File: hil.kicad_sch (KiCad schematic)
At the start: 29 parts, among them J1 5V In, J10 +3V3, J11 GND, J2 USB_B, J3 IO A, J4 IO B, J7 CAN, J8 I2C, J9 +5V, U1 MCP2515, U2 AZ1117-3.3, U3 MCP2562, Y1 16 MHz

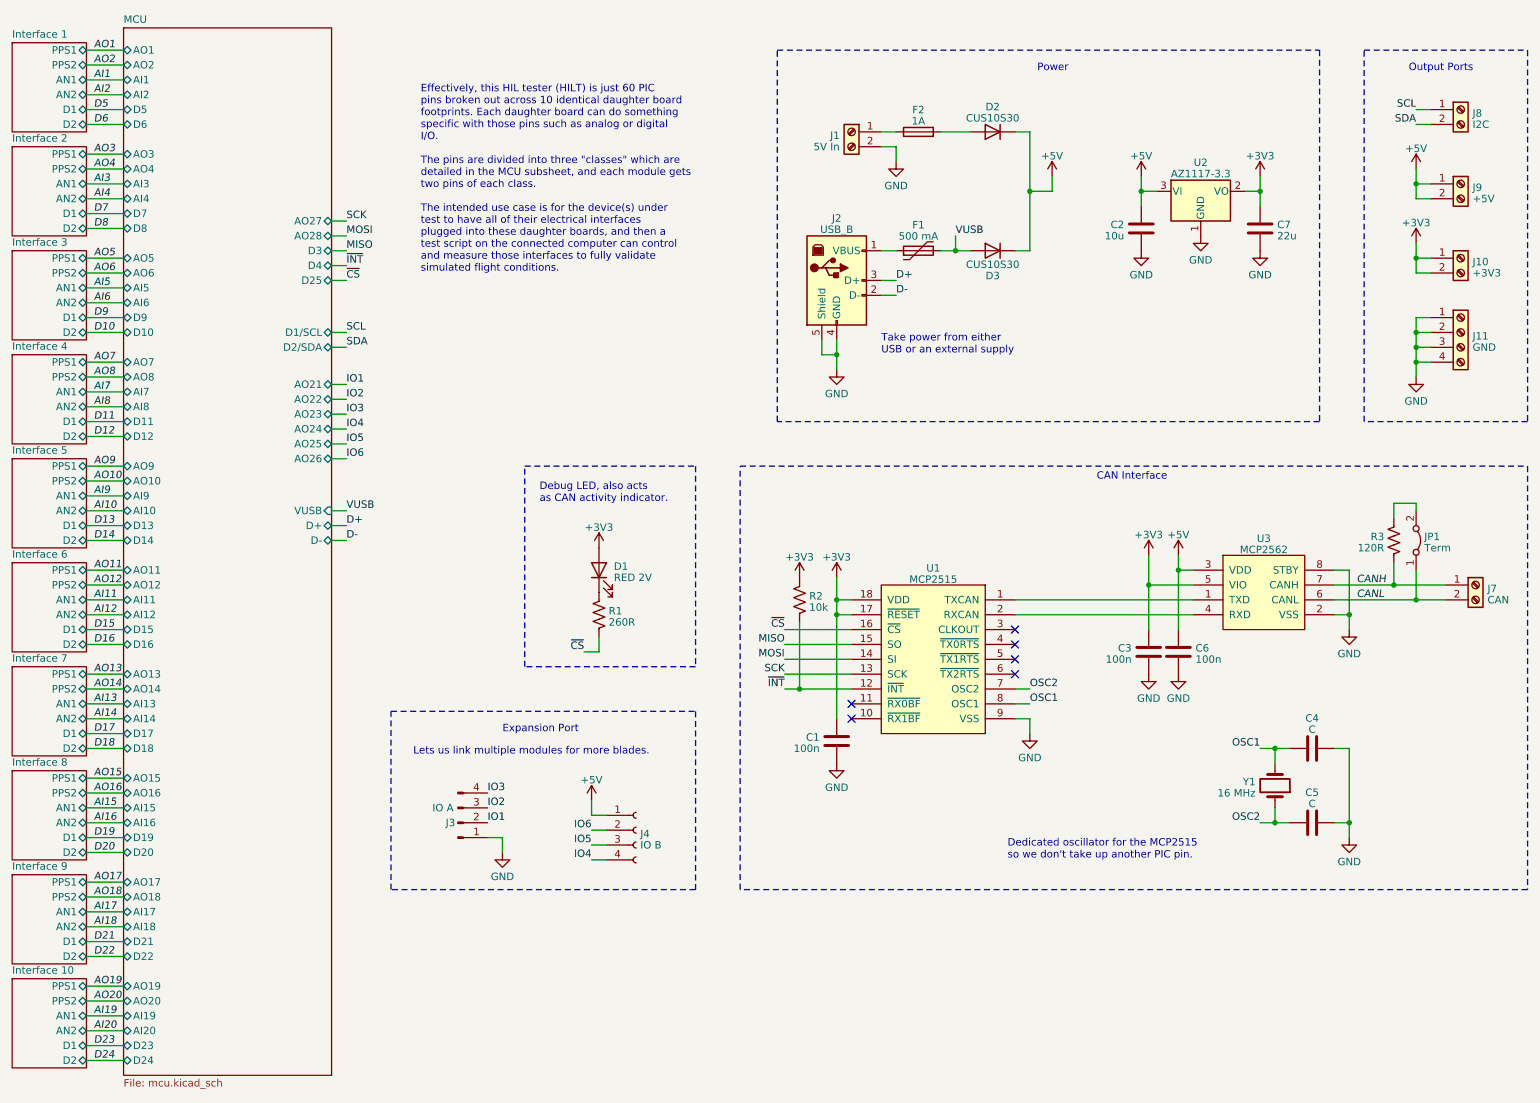
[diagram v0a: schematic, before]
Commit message: Address review comments, finish routing HILT main board
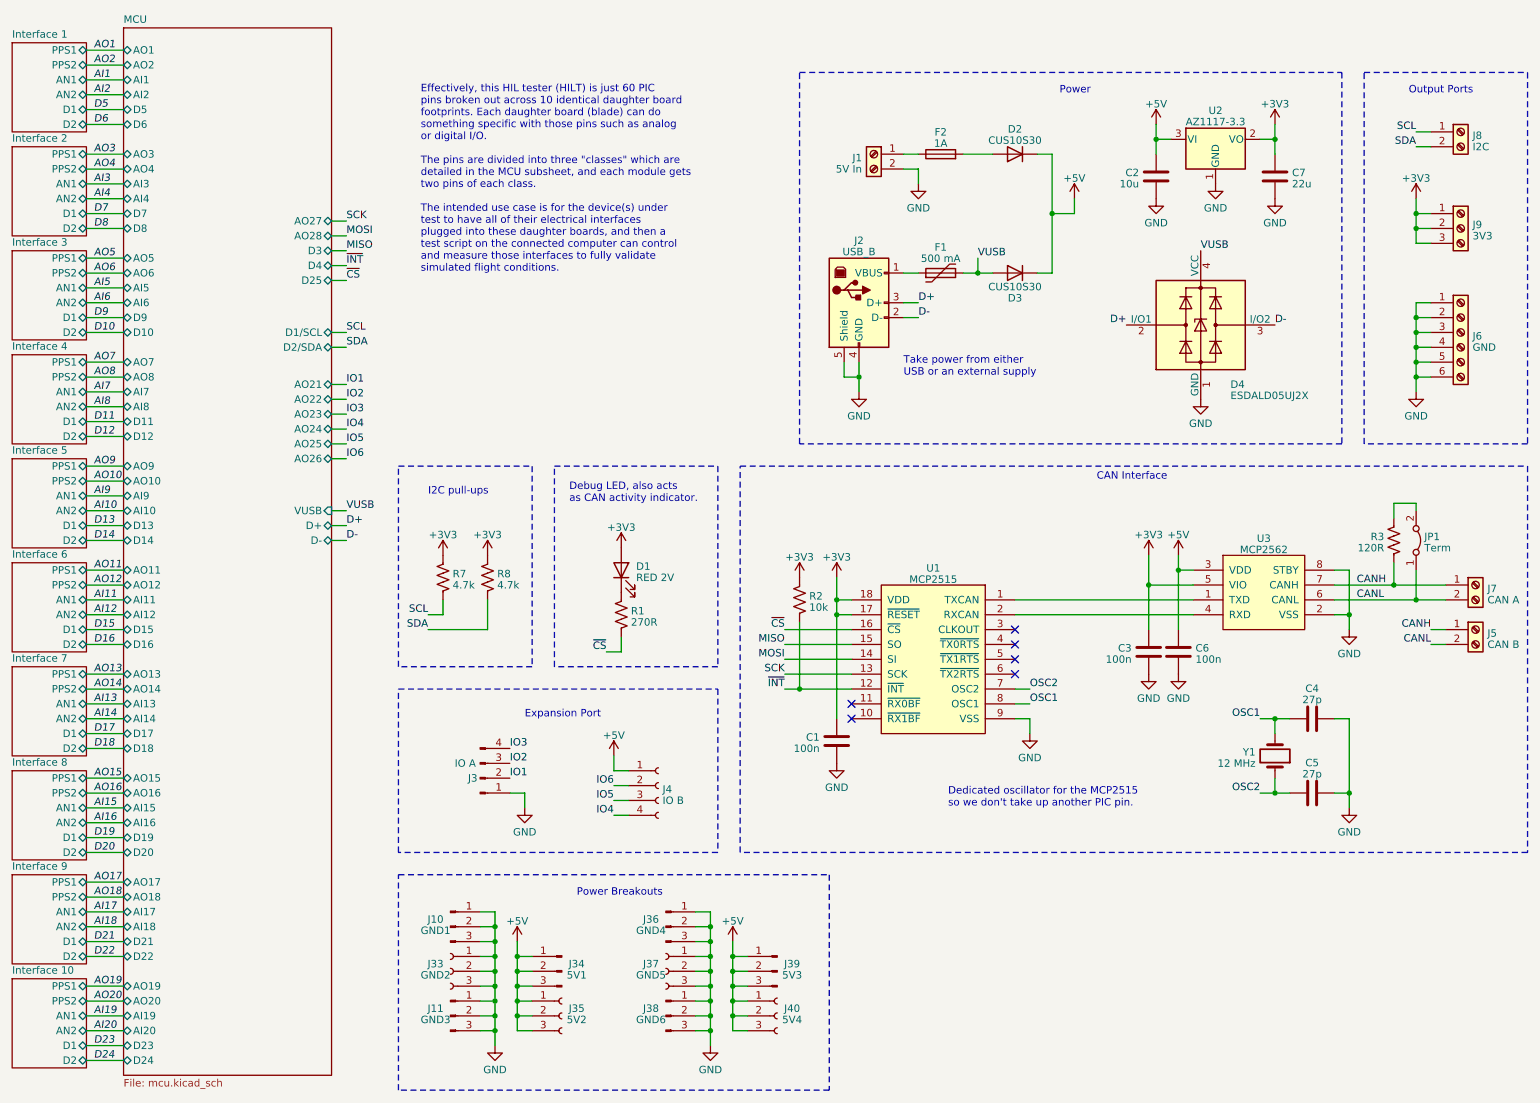
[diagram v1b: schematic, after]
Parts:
- removed J10: +3V3, TerminalBlock_Phoenix:TerminalBlock_Phoenix_PT-1,5-2-5.0-H_1x02_P5.00mm_Horizontal, symbol Connector:Screw_Terminal_01x02
- removed J11: GND, TerminalBlock_Phoenix:TerminalBlock_Phoenix_PT-1,5-4-5.0-H_1x04_P5.00mm_Horizontal, symbol Connector:Screw_Terminal_01x04
- removed J9: +5V, TerminalBlock_Phoenix:TerminalBlock_Phoenix_PT-1,5-2-5.0-H_1x02_P5.00mm_Horizontal, symbol Connector:Screw_Terminal_01x02
- added D4: ESDALD05UJ2X, Package_TO_SOT_SMD:SOT-143_Handsoldering, symbol Power_Protection:PRTR5V0U2X
- added J10: GND1, Connector_PinHeader_2.54mm:PinHeader_1x03_P2.54mm_Horizontal, symbol Connector:Conn_01x03_Pin
- added J11: GND3, Connector_PinHeader_2.54mm:PinHeader_1x03_P2.54mm_Horizontal, symbol Connector:Conn_01x03_Pin
- added J33: GND2, Connector_Harwin:Harwin_M20-89003xx_1x03_P2.54mm_Horizontal, symbol Connector:Conn_01x03_Socket
- added J34: 5V1, Connector_PinHeader_2.54mm:PinHeader_1x03_P2.54mm_Horizontal, symbol Connector:Conn_01x03_Pin
- added J35: 5V2, Connector_PinSocket_2.54mm:PinSocket_1x03_P2.54mm_Horizontal, symbol Connector:Conn_01x03_Socket
- added J36: GND4, Connector_PinHeader_2.54mm:PinHeader_1x03_P2.54mm_Horizontal, symbol Connector:Conn_01x03_Pin
- added J37: GND5, Connector_PinSocket_2.54mm:PinSocket_1x03_P2.54mm_Horizontal, symbol Connector:Conn_01x03_Socket
- added J38: GND6, Connector_PinHeader_2.54mm:PinHeader_1x03_P2.54mm_Horizontal, symbol Connector:Conn_01x03_Pin
- added J39: 5V3, Connector_PinHeader_2.54mm:PinHeader_1x03_P2.54mm_Horizontal, symbol Connector:Conn_01x03_Pin
- added J40: 5V4, Connector_PinSocket_2.54mm:PinSocket_1x03_P2.54mm_Horizontal, symbol Connector:Conn_01x03_Socket
- added J5: CAN B, TerminalBlock_Phoenix:TerminalBlock_Phoenix_PT-1,5-2-3.5-H_1x02_P3.50mm_Horizontal, symbol Connector:Screw_Terminal_01x02
- added J6: GND, TerminalBlock_Phoenix:TerminalBlock_Phoenix_PT-1,5-6-3.5-H_1x06_P3.50mm_Horizontal, symbol Connector:Screw_Terminal_01x06
- added J9: 3V3, TerminalBlock_Phoenix:TerminalBlock_Phoenix_PT-1,5-3-3.5-H_1x03_P3.50mm_Horizontal, symbol Connector:Screw_Terminal_01x03
- added R7, R8: 4.7k, Resistor_SMD:R_0805_2012Metric_Pad1.20x1.40mm_HandSolder, symbol Device:R_US
- C4, C5: value C -> 27p
- J7: value CAN -> CAN A; footprint TerminalBlock_Phoenix:TerminalBlock_Phoenix_PT-1,5-2-5.0-H_1x02_P5.00mm_Horizontal -> TerminalBlock_Phoenix:TerminalBlock_Phoenix_PT-1,5-2-3.5-H_1x02_P3.50mm_Horizontal
- J8: footprint TerminalBlock_Phoenix:TerminalBlock_Phoenix_PT-1,5-2-5.0-H_1x02_P5.00mm_Horizontal -> TerminalBlock_Phoenix:TerminalBlock_Phoenix_PT-1,5-2-3.5-H_1x02_P3.50mm_Horizontal
- R1: value 260R -> 270R
- Y1: value 16 MHz -> 12 MHz
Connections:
- net +3V3: now also J9.1 (Pin_1), J9.2 (Pin_2), J9.3 (Pin_3), R7.1, R8.1
- net +5V: now also J34.1 (Pin_1), J34.2 (Pin_2), J34.3 (Pin_3), J35.1 (Pin_1), J35.2 (Pin_2), J35.3 (Pin_3), J39.1 (Pin_1), J39.2 (Pin_2), J39.3 (Pin_3), J40.1 (Pin_1), J40.2 (Pin_2), J40.3 (Pin_3)
- net CANH: now also J5.1 (Pin_1)
- net CANL: now also J5.2 (Pin_2)
- net D+: now also D4.2 (I/O1)
- net D-: now also D4.3 (I/O2)
- net GND: now also D4.1 (GND), J10.1 (Pin_1), J10.2 (Pin_2), J10.3 (Pin_3), J11.1 (Pin_1), J11.2 (Pin_2), J11.3 (Pin_3), J33.1 (Pin_1), J33.2 (Pin_2), J33.3 (Pin_3), J36.1 (Pin_1), J36.2 (Pin_2), J36.3 (Pin_3), J37.1 (Pin_1), J37.2 (Pin_2), J37.3 (Pin_3), J38.1 (Pin_1), J38.2 (Pin_2), J38.3 (Pin_3), J6.1 (Pin_1), J6.2 (Pin_2), J6.3 (Pin_3), J6.4 (Pin_4), J6.5 (Pin_5), J6.6 (Pin_6)
- net SCL: now also R7.2
- net SDA: now also R8.2
- net VUSB: now also D4.4 (VCC)
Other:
- note added: "Effectively, this HIL tester (HILT) is just 60 PIC pins broken out across 10 identical daughter board footprints. Each daughter board (blade) can do something specific with those pins such as analog or digital I/O. The pins are divided into three "classes" which are detailed in the MCU subsheet, and each module gets two pins of each class. The intended use case is for the device(s) under test to 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"
- note added: "I2C pull-ups"
- note added: "Power Breakouts"
- note removed: "Effectively, this HIL tester (HILT) is just 60 PIC pins broken out across 10 identical daughter board footprints. Each daughter board can do something specific with those pins such as analog or digital I/O. The pins are divided into three "classes" which are detailed in the MCU subsheet, and each module gets two pins of each class. The intended use case is for the device(s) under test to have all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"
- note removed: "Lets us link multiple modules for more blades."
- moved on the sheet: C2, C4, C5, C7, D1, D2, D3, F1, F2, J1, J2, J3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
